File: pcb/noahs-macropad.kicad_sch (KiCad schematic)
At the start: 17 parts, among them U1 MOUDLE-SEEEDUINO-XIAO

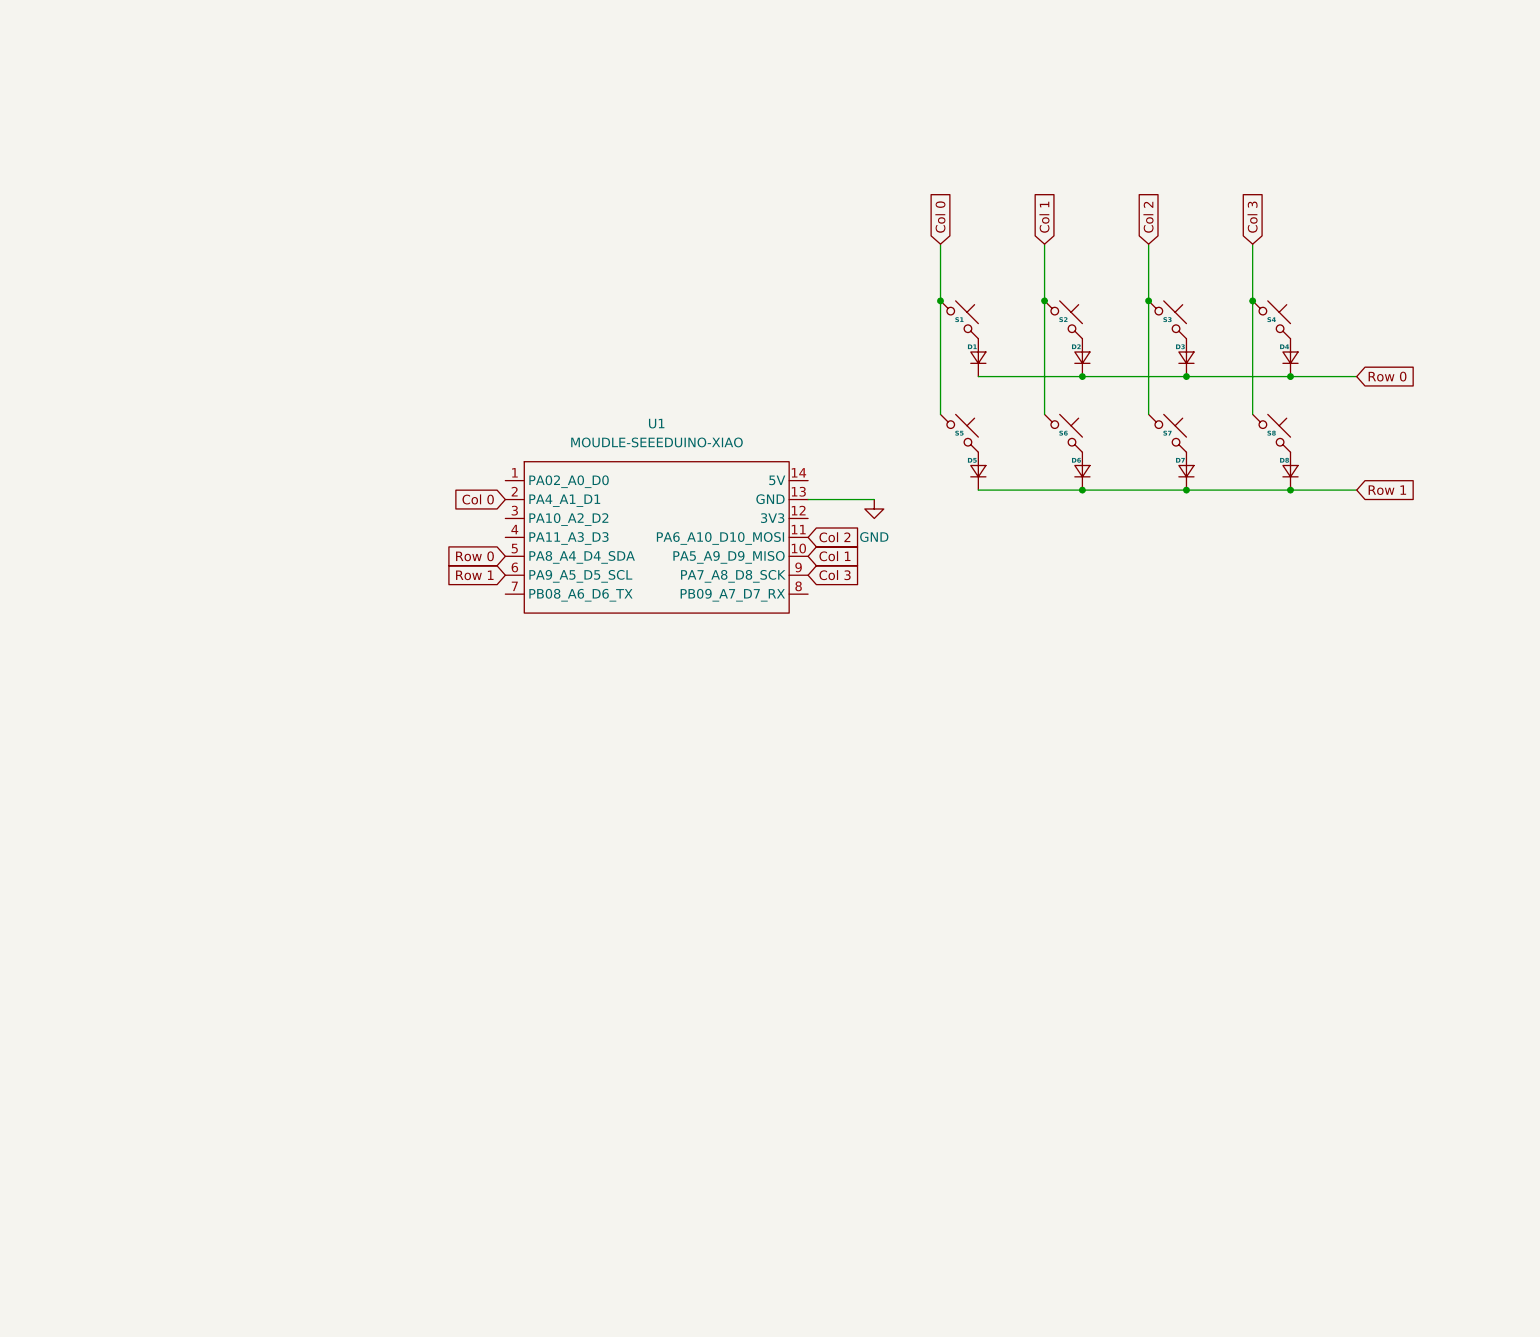
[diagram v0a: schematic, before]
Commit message: redesign with oled screen
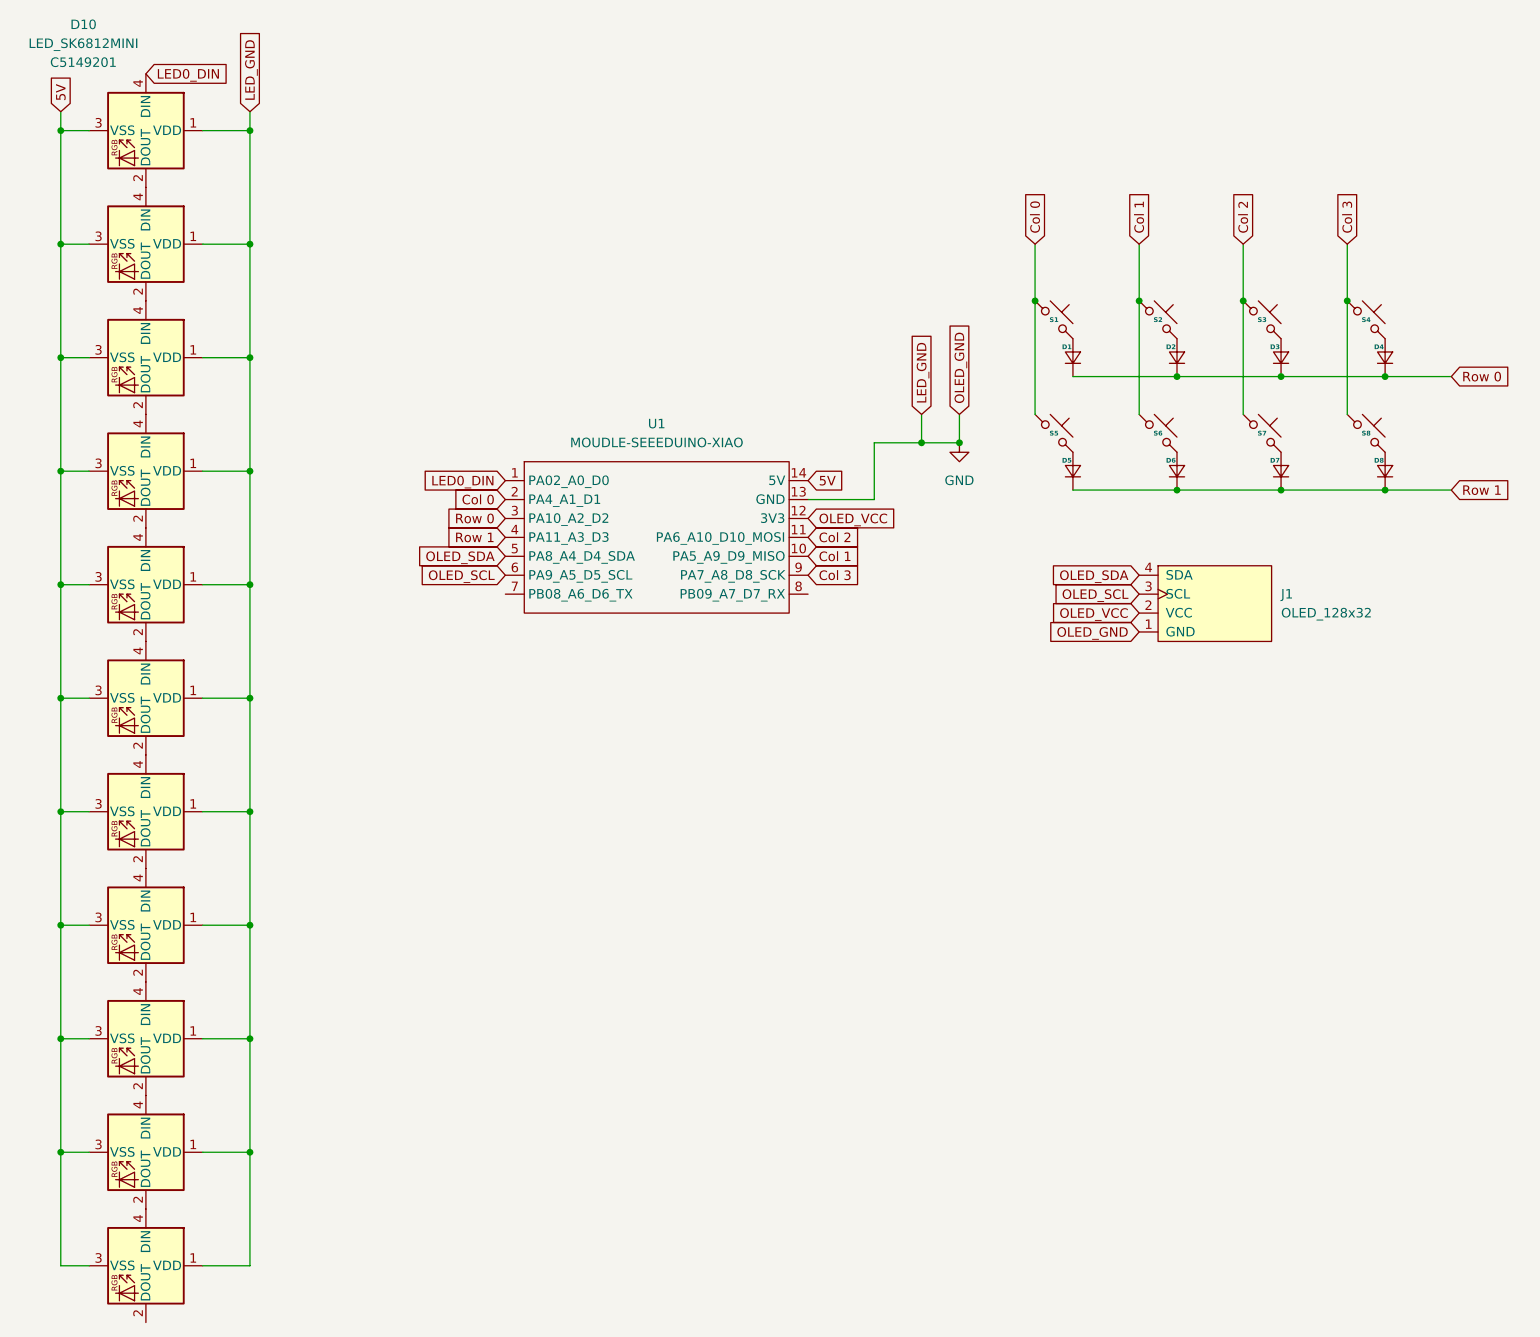
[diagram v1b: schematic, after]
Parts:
- added D10, D11, D12, D13, D14, D15, D16, D17, D18, D19, D9: LED_SK6812MINI, ScottoKeebs_Components:LED_SK6812MINI, symbol ScottoKeebs:LED_SK6812MINI
- added J1: OLED_128x32, ScottoKeebs_Components:OLED_128x32, symbol ScottoKeebs:OLED_128x32
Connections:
- net GND: now also D10.1 (VDD), D11.1 (VDD), D12.1 (VDD), D13.1 (VDD), D14.1 (VDD), D15.1 (VDD), D16.1 (VDD), D17.1 (VDD), D18.1 (VDD), D19.1 (VDD), D9.1 (VDD), J1.1 (GND)
- net Row 0: now also U1.3 (PA10_A2_D2); no longer U1.5 (PA8_A4_D4_SDA)
- net Row 1: now also U1.4 (PA11_A3_D3); no longer U1.6 (PA9_A5_D5_SCL)
- net LED0_DIN: now reaches U1.1 (PA02_A0_D0)
- net LED0_DIN: now also D10.4 (DIN)
- net OLED_VCC: now reaches U1.12 (3V3)
- net OLED_VCC: now also J1.2 (VCC)
- net 5V: now reaches U1.14 (5V)
- net 5V: now also D10.3 (VSS), D11.3 (VSS), D12.3 (VSS), D13.3 (VSS), D14.3 (VSS), D15.3 (VSS), D16.3 (VSS), D17.3 (VSS), D18.3 (VSS), D19.3 (VSS), D9.3 (VSS)
- new net: D10.2 (DOUT), D9.4 (DIN)
- new net: D14.2 (DOUT), D15.4 (DIN)
- new net: D13.2 (DOUT), D14.4 (DIN)
- new net: D16.2 (DOUT), D17.4 (DIN)
- new net: D15.2 (DOUT), D16.4 (DIN)
- new net: D17.2 (DOUT), D18.4 (DIN)
- new net: D12.2 (DOUT), D13.4 (DIN)
- new net: D11.2 (DOUT), D12.4 (DIN)
- new net: D18.2 (DOUT), D19.4 (DIN)
- new net: D11.4 (DIN), D9.2 (DOUT)
- new net OLED_SCL: J1.3 (SCL), U1.6 (PA9_A5_D5_SCL)
- new net OLED_SDA: J1.4 (SDA), U1.5 (PA8_A4_D4_SDA)
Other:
- moved on the sheet: D1, D2, D3, D4, D5, D6, D7, D8, S1, S2, S3, S4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
